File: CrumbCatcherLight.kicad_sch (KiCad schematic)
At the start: 43 parts, among them J1 USB_C_Receptacle_USB2.0, SW1 SW_SPST, SW10 SW_SPST, SW11 SW_SPST, SW12 SW_SPST, SW15 Rotary, SW16 SW_SPST, SW17 SW_SPST, SW18 SW_SPST, SW19 SW_SPST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

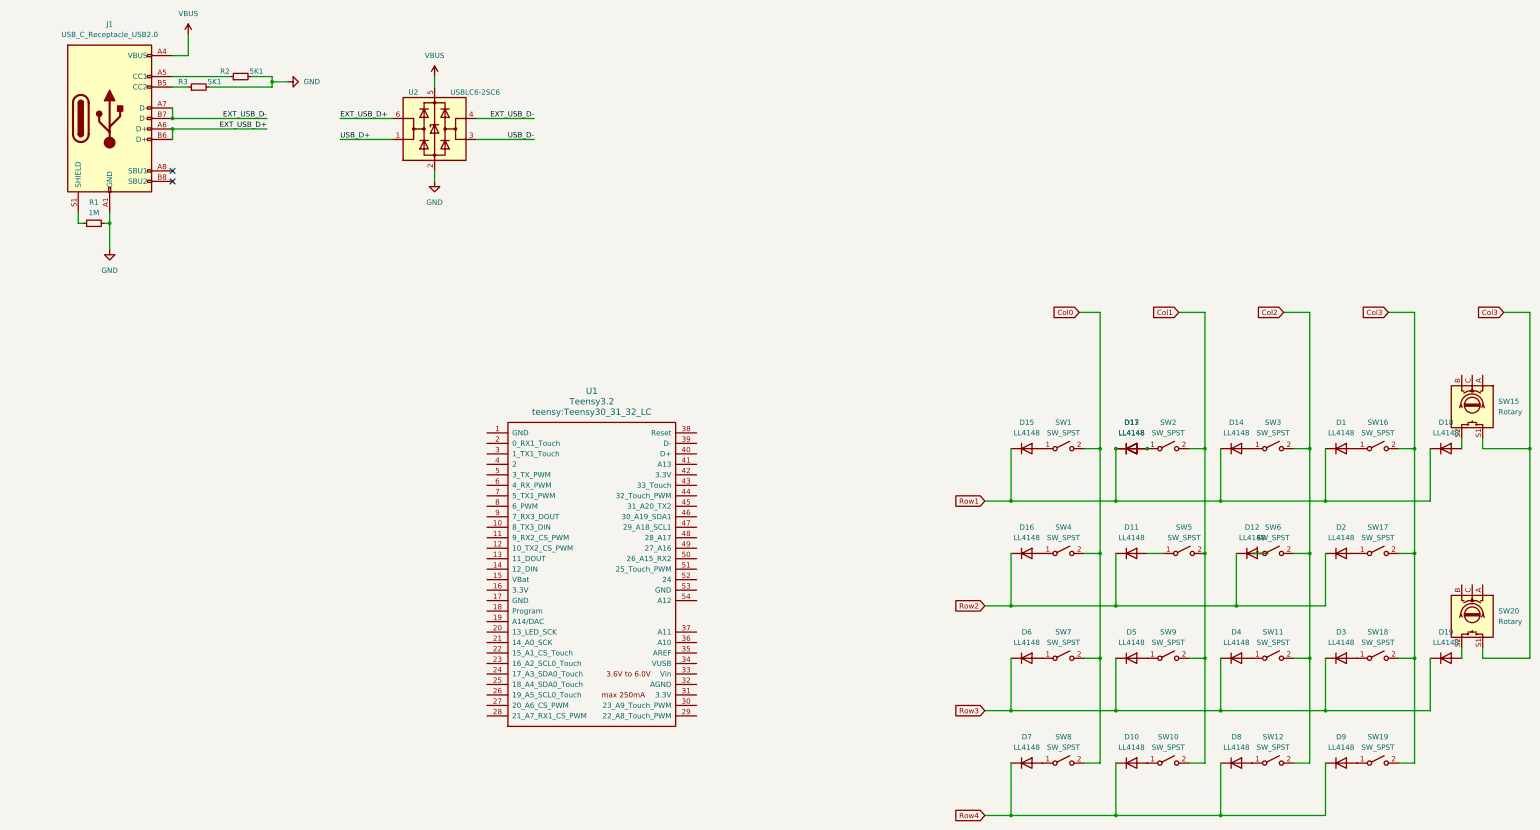
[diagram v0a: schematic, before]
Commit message: Add MCU, remove teensy, separate sections into sheets
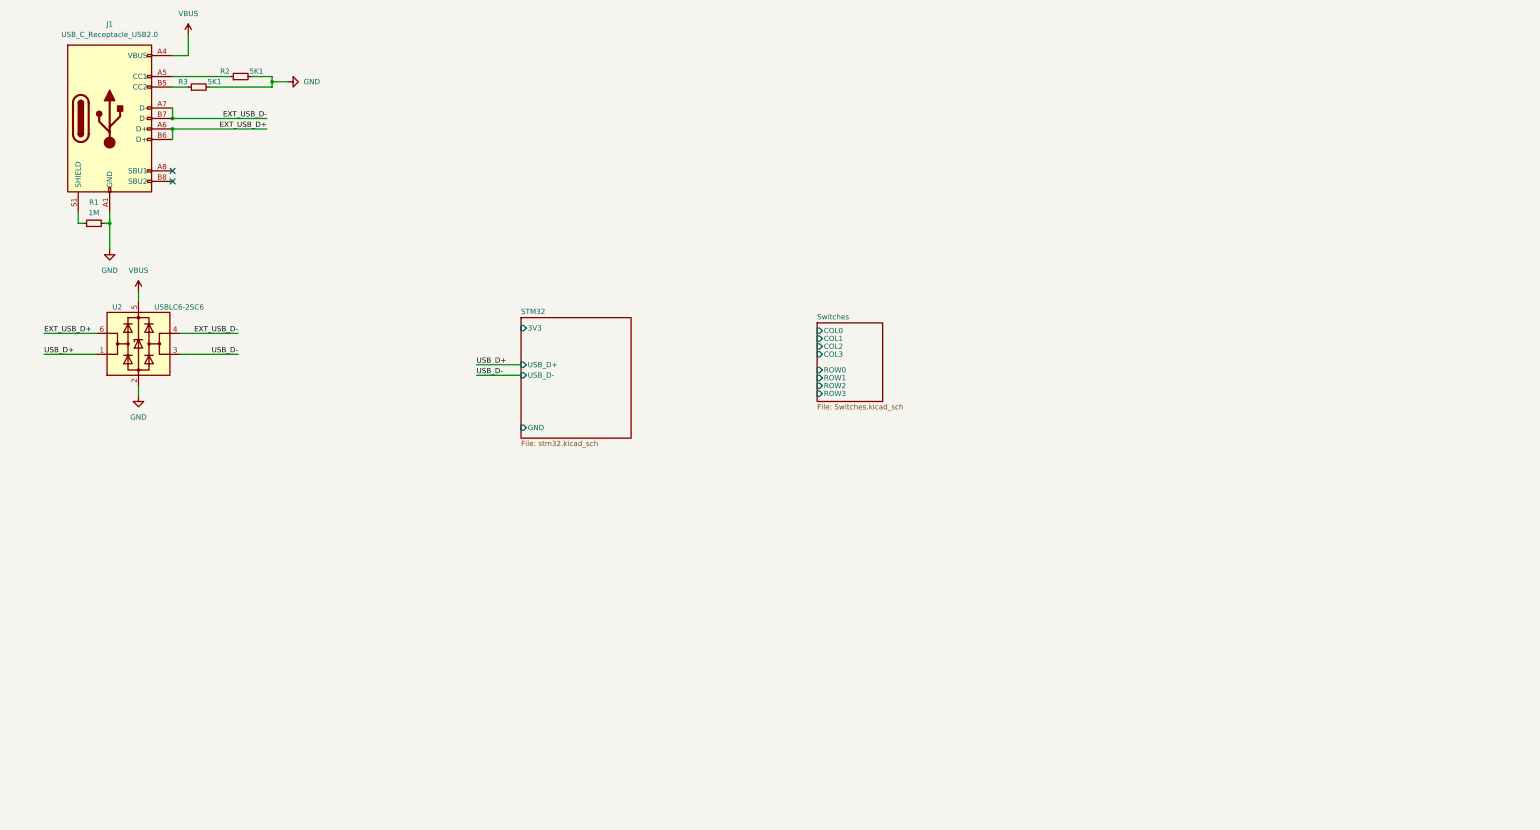
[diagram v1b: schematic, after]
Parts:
- removed D1, D10, D11, D12, D13, D14, D15, D16, D17, D18, D19, D2, D3, D4, D5, D6, D7, D8, D9: LL4148, Diode_SMD:D_MiniMELF, symbol Diode:LL4148
- removed SW1, SW10, SW11, SW12, SW16, SW17, SW18, SW19, SW2, SW3, SW4, SW5, SW6, SW7, SW8, SW9: SW_SPST, PCM_Switch_Keyboard_Cherry_MX:SW_Cherry_MX_PCB_1.00u, symbol Switch:SW_SPST
- removed SW15, SW20: Rotary, symbol Device:RotaryEncoder_Switch
- removed U1: Teensy3.2, teensy:Teensy30_31_32_LC, symbol teensy:Teensy3.2
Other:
- added sheet STM32 (stm32.kicad_sch)
- added sheet Switches (Switches.kicad_sch)
- moved on the sheet: U2

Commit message: Add stm crystal, update title block, add power on LED for 3V3 line
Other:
- company: (none) -> MadMan
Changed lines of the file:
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@@
   (title_block
     (title "Crumb Catcher")
-    (date "2023-10-18")
+    (date "2023-10-25")
     (rev "A")
+    (company "MadMan")
   )
   (junction (at 50.8 44.45) (diameter 0) (color 0 0 0 0)

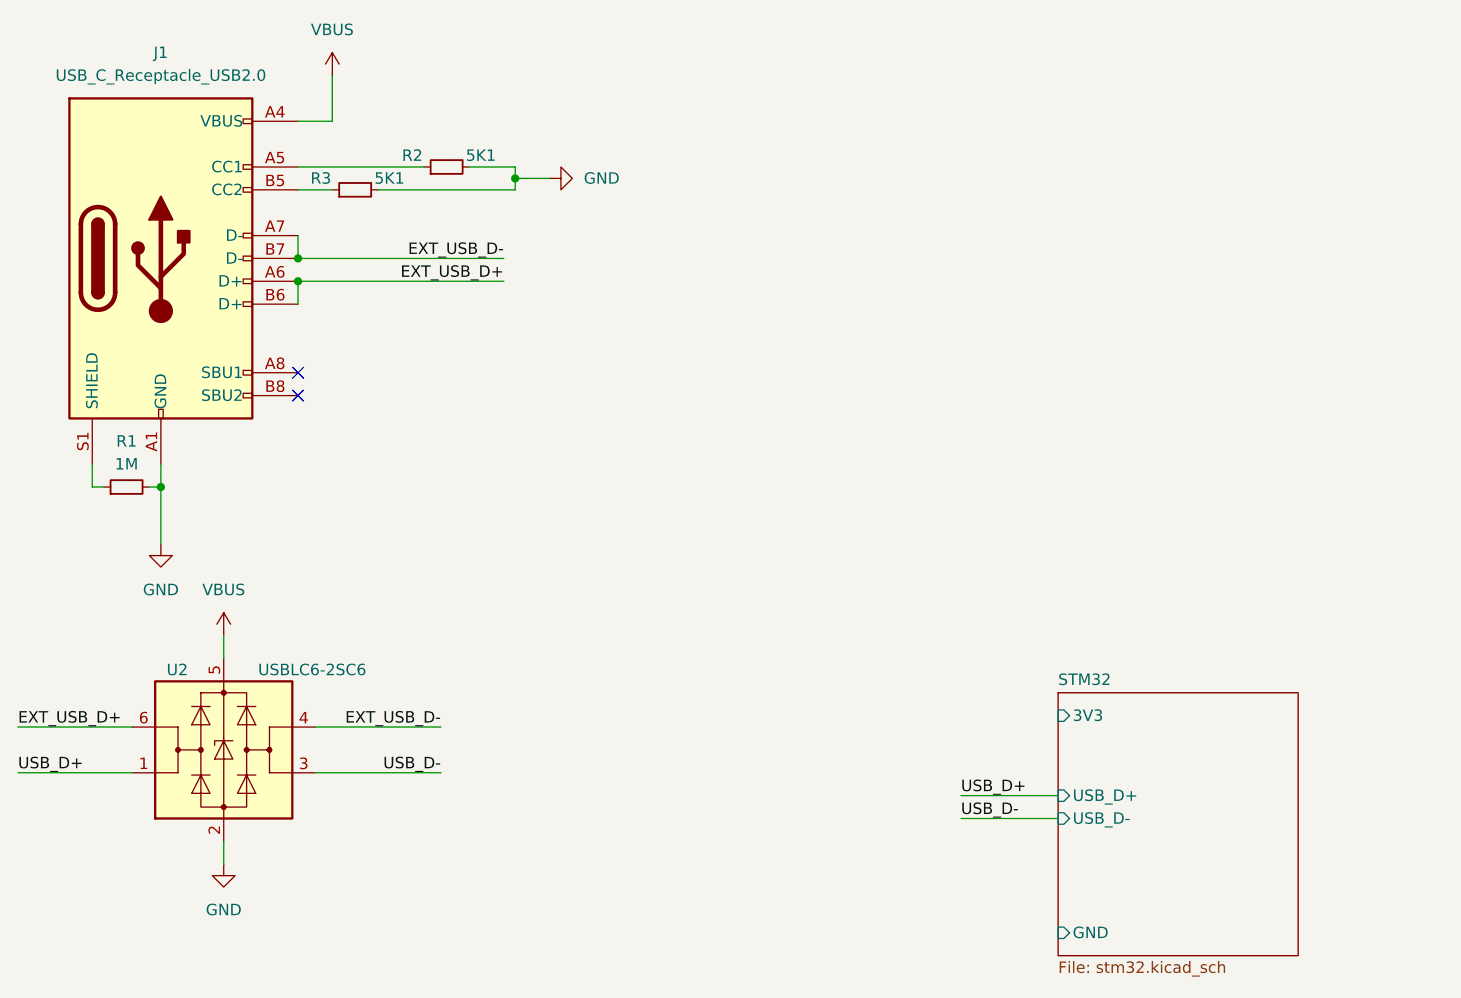
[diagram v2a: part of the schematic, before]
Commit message: Cleanup, Add usb emc and esd
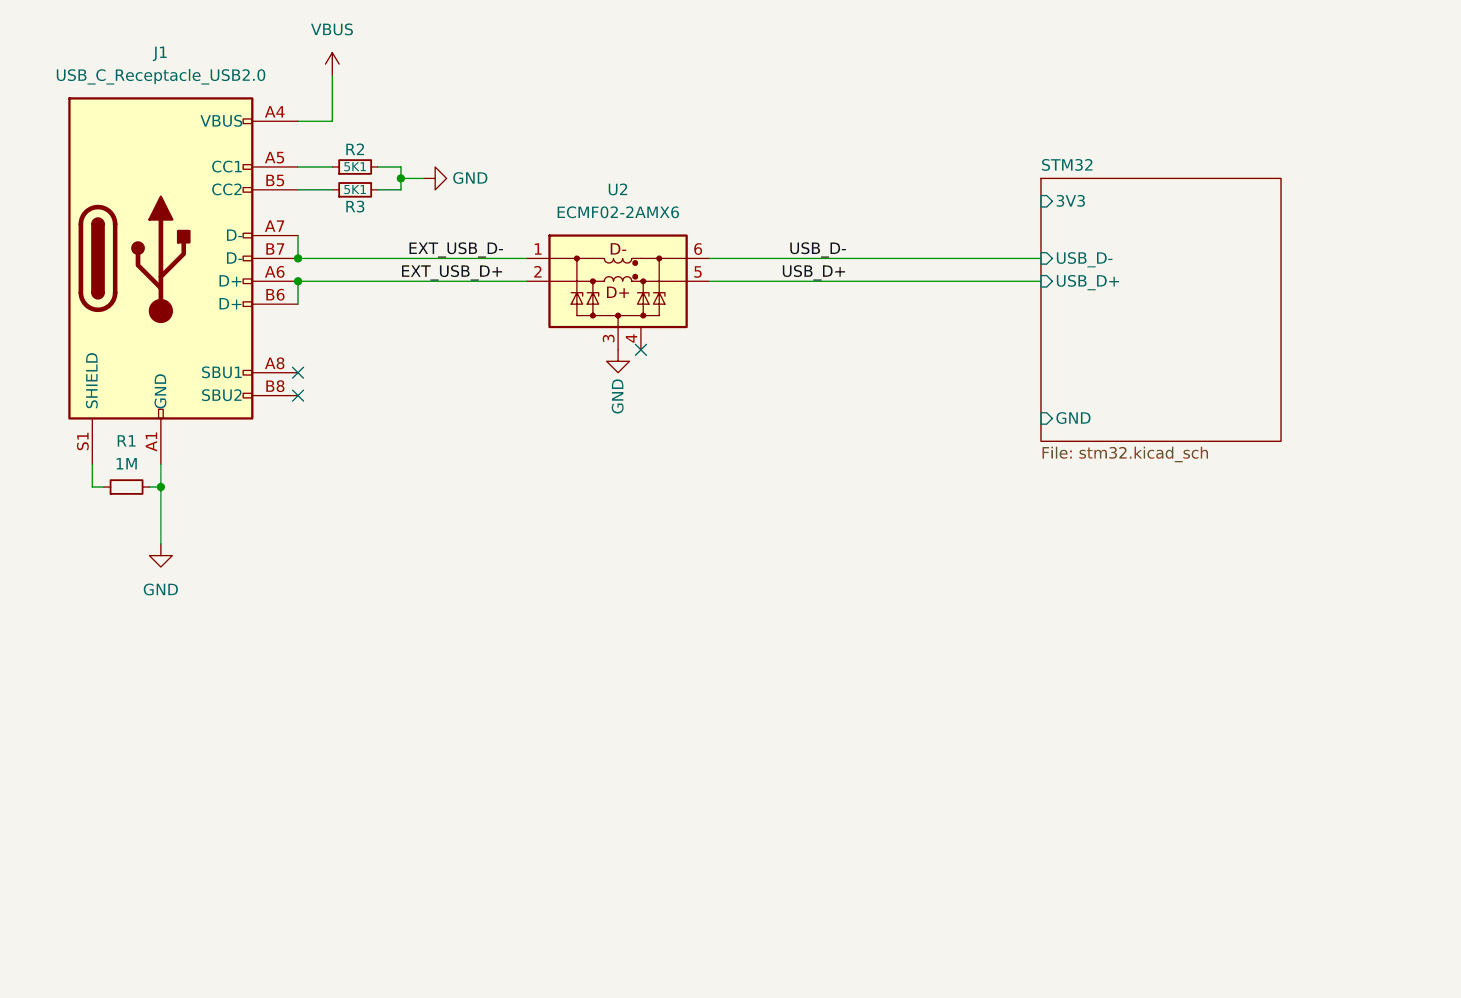
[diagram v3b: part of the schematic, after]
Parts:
- removed U2: USBLC6-2SC6, Package_TO_SOT_SMD:SOT-23-6, symbol Power_Protection:USBLC6-2SC6
- added U2: ECMF02-2AMX6, Package_DFN_QFN:ST_UQFN-6L_1.5x1.7mm_P0.5mm, symbol Local:ECMF02-2AMX6
- J1: footprint (none) -> Connector_USB:USB_C_Receptacle_GCT_USB4105-xx-A_16P_TopMnt_Horizontal
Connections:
- net EXT_USB_D+: now also U2.2 (D-_in)
- net EXT_USB_D-: now also U2.1 (D+_in)
- net GND: now also U2.3 (GND)
- net USB_D+: now also U2.5 (D-_out)
- net USB_D-: now also U2.6 (D+_out)
- no-connect marks 2 -> 3
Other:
- moved on the sheet: R2

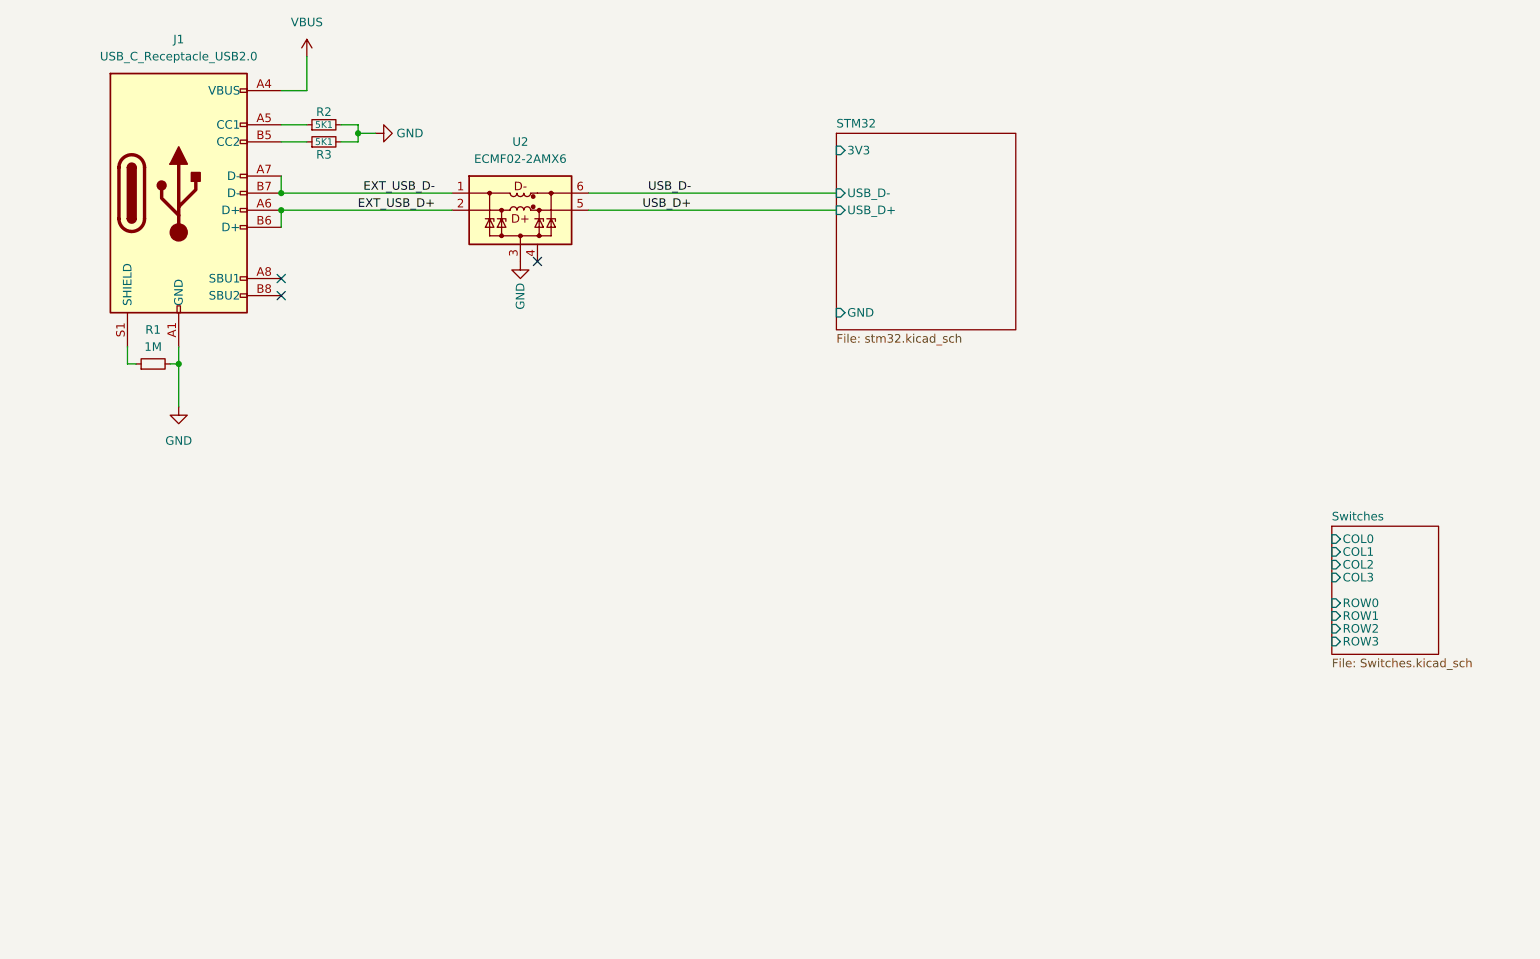
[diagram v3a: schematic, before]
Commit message: Update BOM, start to fill in part metadata
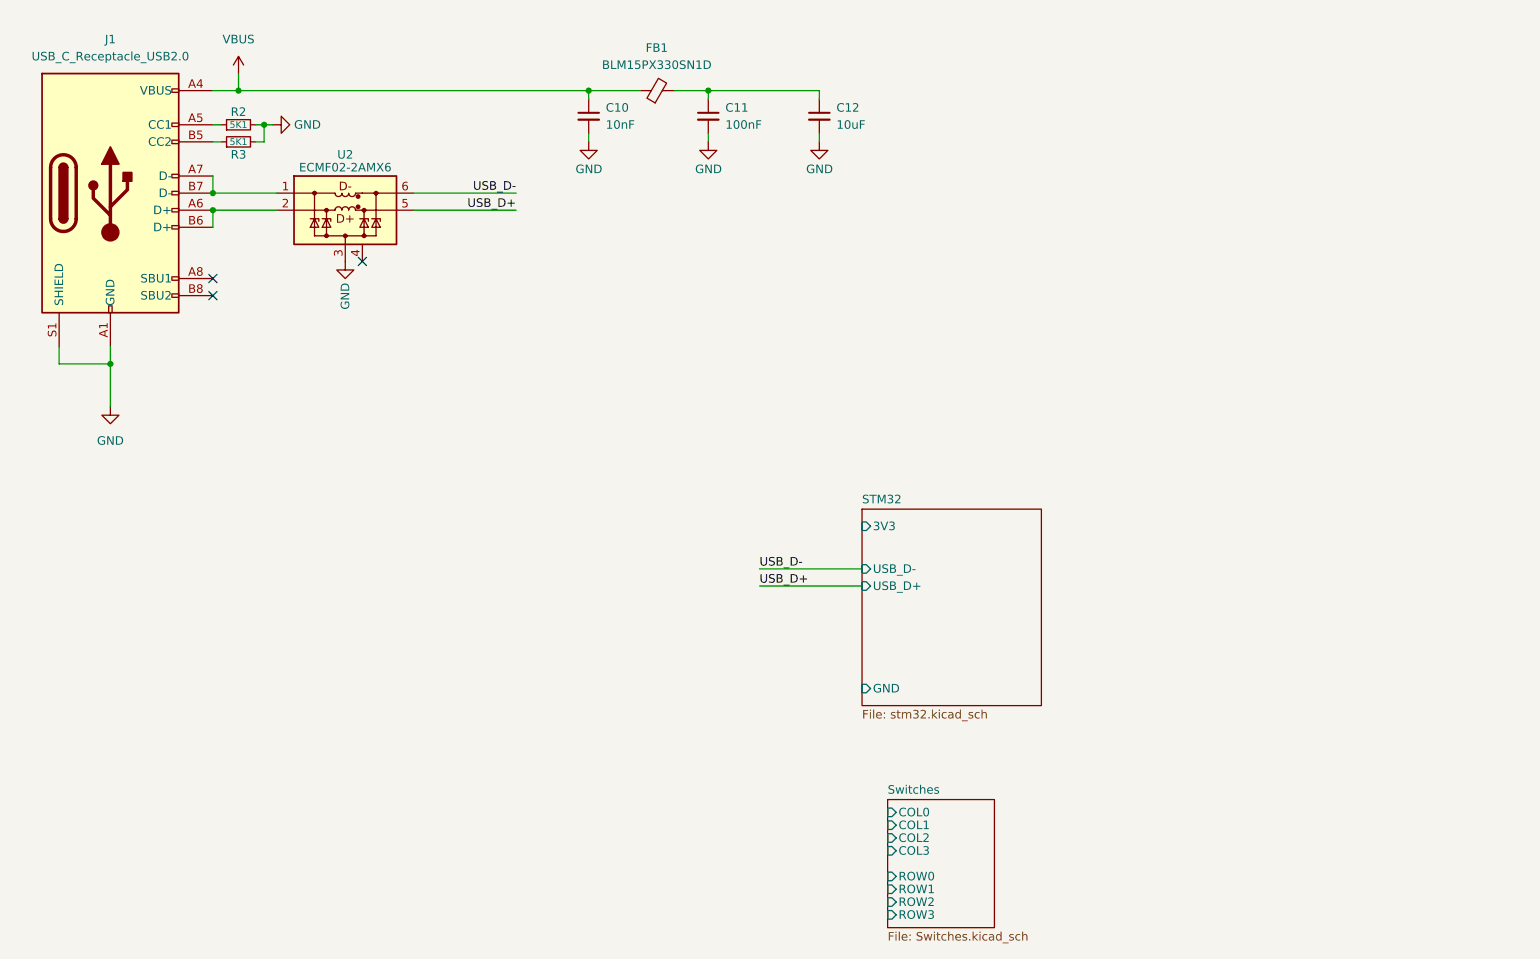
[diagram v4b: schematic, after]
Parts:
- removed R1: 1M, Resistor_SMD:R_0603_1608Metric, symbol Device:R_Small
- added C10: 10nF, Capacitor_SMD:C_0402_1005Metric, symbol Device:C_Small
- added C11: 100nF, Capacitor_SMD:C_0402_1005Metric, symbol Device:C_Small
- added C12: 10uF, Capacitor_SMD:C_0805_2012Metric, symbol Device:C_Small
- added FB1: BLM15PX330SN1D, Inductor_SMD:L_0402_1005Metric, symbol Device:FerriteBead_Small
- R2, R3: footprint Resistor_SMD:R_0603_1608Metric -> Resistor_SMD:R_0402_1005Metric; MPN (none) -> RC0402FR-075K1L; Manufacturer (none) -> YAGEO; Price (none) -> $0.16; Rating (none) -> RES 5.1K OHM 1% 1/16W 0402; Supplier (none) -> Digikey; Supplier PN (none) -> 311-5.10KLRCT-ND
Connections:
- net GND: now also J1.S1 (SHIELD), C10.2, C11.2, C12.2
- net VBUS: now also C10.1, FB1.1
- net EXT_USB_D+: no longer names the net of J1.A6 (D+), J1.B6 (D+), U2.2 (D-_in)
- net EXT_USB_D-: no longer names the net of J1.A7 (D-), J1.B7 (D-), U2.1 (D+_in)
- new net: C11.1, C12.1, FB1.2
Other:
- moved on the sheet: J1, R2, R3, U2

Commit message: Add LDO and other minor updates
LP38691
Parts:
- added C13: 10uF, Capacitor_SMD:C_0805_2012Metric, symbol Device:C_Small
- added U3: LP38691SD-3.3, Package_SON:WSON-6-1EP_3x3mm_P0.95mm, symbol Regulator_Linear:LP38691SD-3.3
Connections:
- net GND: now also C13.2, U3.2 (GND), U3.7 (EP)
- net at C11.1, C12.1, FB1.2: now also U3.1 (IN), U3.6 (IN)
- new net +3V3: C13.1, U3.4 (OUT), U3.5 (SNS)
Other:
- moved on the sheet: C10, C11, C12

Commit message: Project cleanup
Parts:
- U3: value LP38691SD-3.3 -> LP38691SDX-3.3; MPN (none) -> LP38691SDX-3.3/NOPB; Manufacturer (none) -> Texas Instruments; Price (none) -> $2.40; Rating (none) -> IC REG LINEAR 3.3V 500MA 6WSON; Supplier (none) -> Digikey; Supplier PN (none) -> 296-LP38691SDX-3.3/NOPBCT-ND
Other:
- sheet STM32 renamed STM32F0
- sheet STM32F0: file stm32.kicad_sch -> mad_lib/schematics/STM32F0.kicad_sch
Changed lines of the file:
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@@
 			)
 		)
-		(property "Value" "LP38691SD-3.3"
+		(property "Value" "LP38691SDX-3.3"
 			(at 165.1 22.86 0)
 			(effects
@@
 			)
 		)
-		(property "Description" "500-mA Low-Dropout CMOS Linear Regulators Stable With Ceramic Output Capacitors, 3.3V output voltage, WSON-6"
+		(property "Description" "Linear Voltage Regulator IC Positive Fixed 1 Output 500mA 6-WSON (3x3)"
+			(at 165.1 29.21 0)
+			(effects
+				(font
+					(size 1.27 1.27)
+				)
+				(hide yes)
+			)
+		)
+		(property "Price" "$2.40"
+			(at 165.1 29.21 0)
+			(effects
+				(font
+					(size 1.27 1.27)
+				)
+				(hide yes)
+			)
+		)
+		(property "Interface" ""
+			(at 165.1 29.21 0)
+			(effects
+				(font
+					(size 1.27 1.27)
+				)
+				(hide yes)
+			)
+		)
+		(property "Rating" "IC REG LINEAR 3.3V 500MA 6WSON"
+			(at 165.1 29.21 0)
+			(effects
+				(font
+					(size 1.27 1.27)
+				)
+				(hide yes)
+			)
+		)
+		(property "Supplier" "Digikey"
+			(at 165.1 29.21 0)
+			(effects
+				(font
+					(size 1.27 1.27)
+				)
+				(hide yes)
+			)
+		)
+		(property "Supplier PN" "296-LP38691SDX-3.3/NOPBCT-ND"
+			(at 165.1 29.21 0)
+			(effects
+				(font
+					(size 1.27 1.27)
+				)
+				(hide yes)
+			)
+		)
+		(property "Manufacturer" "Texas Instruments"
+			(at 165.1 29.21 0)
+			(effects
+				(font
+					(size 1.27 1.27)
+				)
+				(hide yes)
+			)
+		)
+		(property "MPN" "LP38691SDX-3.3/NOPB"
 			(at 165.1 29.21 0)
 			(effects
@@
 			(color 0 0 0 0.0000)
 		)
-		(property "Sheetname" "STM32"
+		(property "Sheetname" "STM32F0"
 			(at 128.27 88.1884 0)
 			(effects
@@
 			)
 		)
-		(property "Sheetfile" "stm32.kicad_sch"
+		(property "Sheetfile" "mad_lib/schematics/STM32F0.kicad_sch"
 			(at 128.27 109.1696 0)
 			(effects
